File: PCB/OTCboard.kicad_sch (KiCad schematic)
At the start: 0 parts

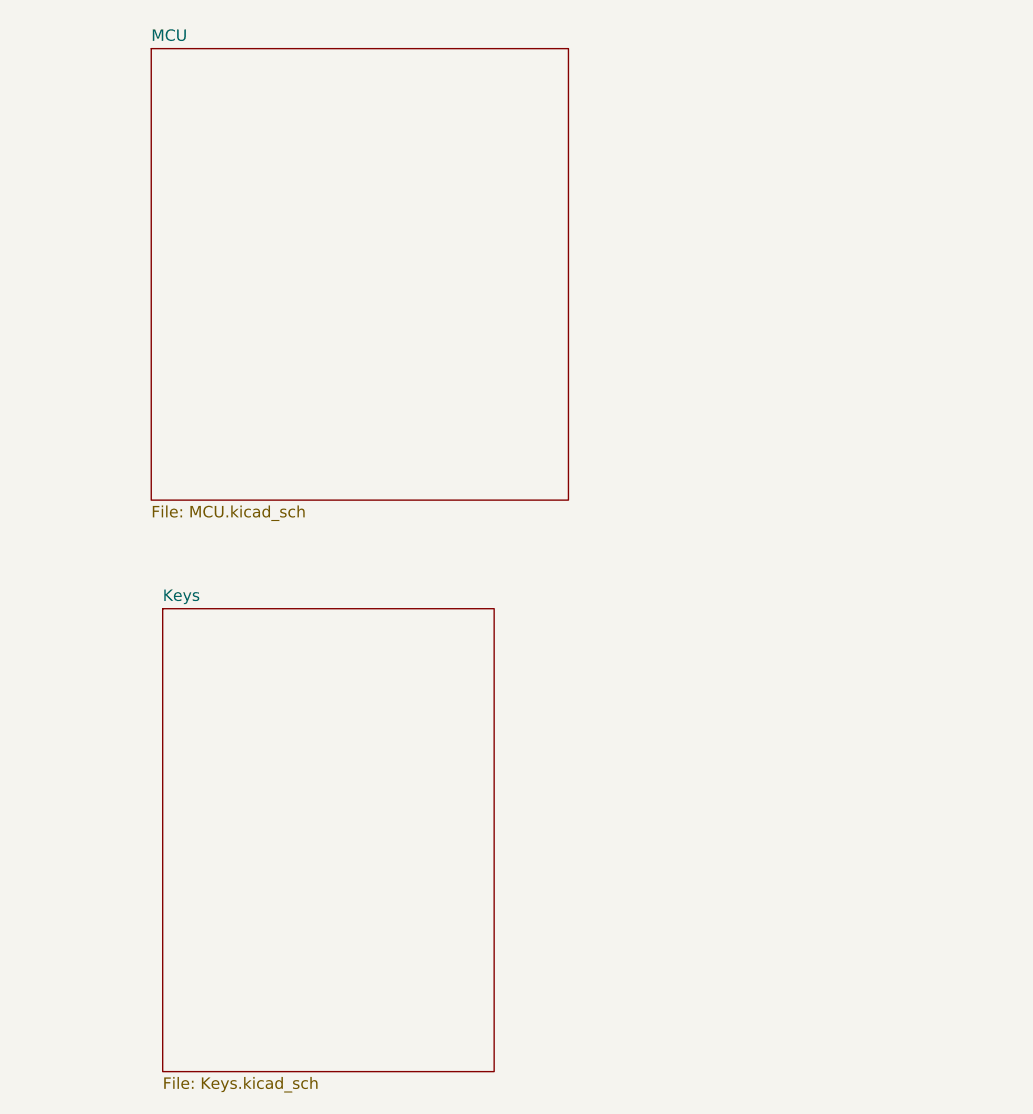
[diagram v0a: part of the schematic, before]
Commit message: switching to hall effect for now
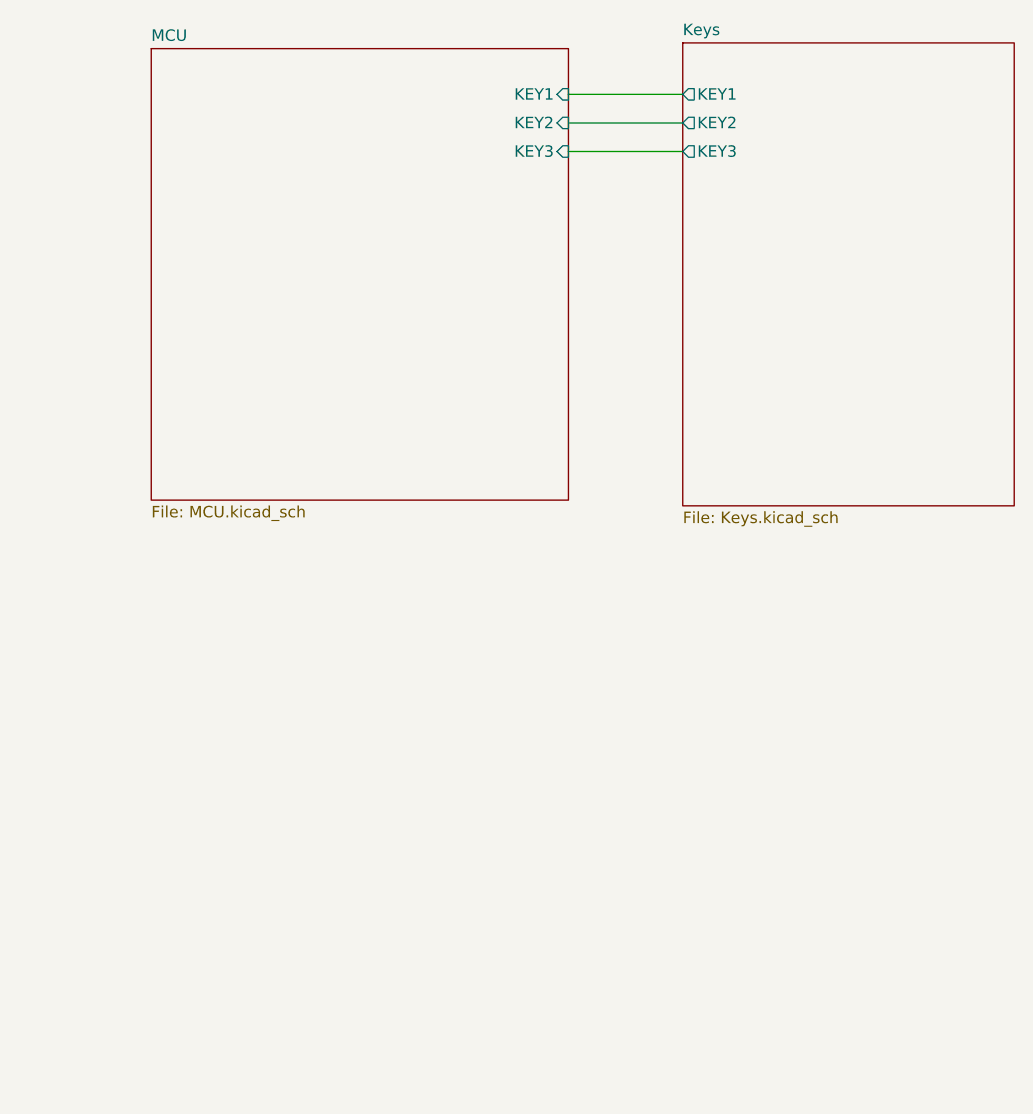
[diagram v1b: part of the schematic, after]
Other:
- sheet Keys ports: added KEY1, KEY2, KEY3; removed none
- sheet MCU ports: added KEY1, KEY2, KEY3; removed none
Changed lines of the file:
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@@
 	(generator_version "9.0")
 	(paper "A4")
+	(wire
+		(pts
+			(xy 137.795 30.48) (xy 150.495 30.48)
+		)
+		(stroke
+			(width 0)
+			(type default)
+		)
+	)
+	(wire
+		(pts
+			(xy 137.795 24.13) (xy 150.495 24.13)
+		)
+		(stroke
+			(width 0)
+			(type default)
+		)
+	)
+	(wire
+		(pts
+			(xy 137.795 27.305) (xy 150.495 27.305)
+		)
+		(stroke
+			(width 0)
+			(type default)
+		)
+	)
 	(sheet
 		(at 91.44 19.05)
@@
 			)
 		)
+		(pin "KEY1" input
+			(at 137.795 24.13 0)
+			(effects
+				(font
+					(size 1.27 1.27)
+				)
+				(justify right)
+			)
+		)
+		(pin "KEY2" input
+			(at 137.795 27.305 0)
+			(effects
+				(font
+					(size 1.27 1.27)
+				)
+				(justify right)
+			)
+		)
+		(pin "KEY3" input
+			(at 137.795 30.48 0)
+			(effects
+				(font
+					(size 1.27 1.27)
+				)
+				(justify right)
+			)
+		)
 		(instances
 			(project "OTCboard"
@@
 	)
 	(sheet
-		(at 92.71 81.28)
+		(at 150.495 18.415)
 		(size 36.83 51.435)
 		(exclude_from_sim no)
@@
 		)
 		(property "Sheetname" "Keys"
-			(at 92.71 80.5684 0)
+			(at 150.495 17.7034 0)
 			(effects
 				(font
@@
 		)
 		(property "Sheetfile" "Keys.kicad_sch"
-			(at 92.71 133.2996 0)
+			(at 150.495 70.4346 0)
 			(effects
 				(font
@@
 			)
 		)
+		(pin "KEY1" output
+			(at 150.495 24.13 180)
+			(effects
+				(font
+					(size 1.27 1.27)
+				)
+				(justify left)
+			)
+		)
+		(pin "KEY2" output
+			(at 150.495 27.305 180)
+			(effects
+				(font
+					(size 1.27 1.27)
+				)
+				(justify left)
+			)
+		)
+		(pin "KEY3" output
+			(at 150.495 30.48 180)
+			(effects
+				(font
+					(size 1.27 1.27)
+				)
+				(justify left)
+			)
+		)

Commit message: cramming for portfolio
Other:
- added sheet LEDs (LEDs.kicad_sch)
- sheet MCU ports: added AddressableLEDs, BL, CS, DC, MOSI, RES, SCK, USB_D+, USB_D-; removed none

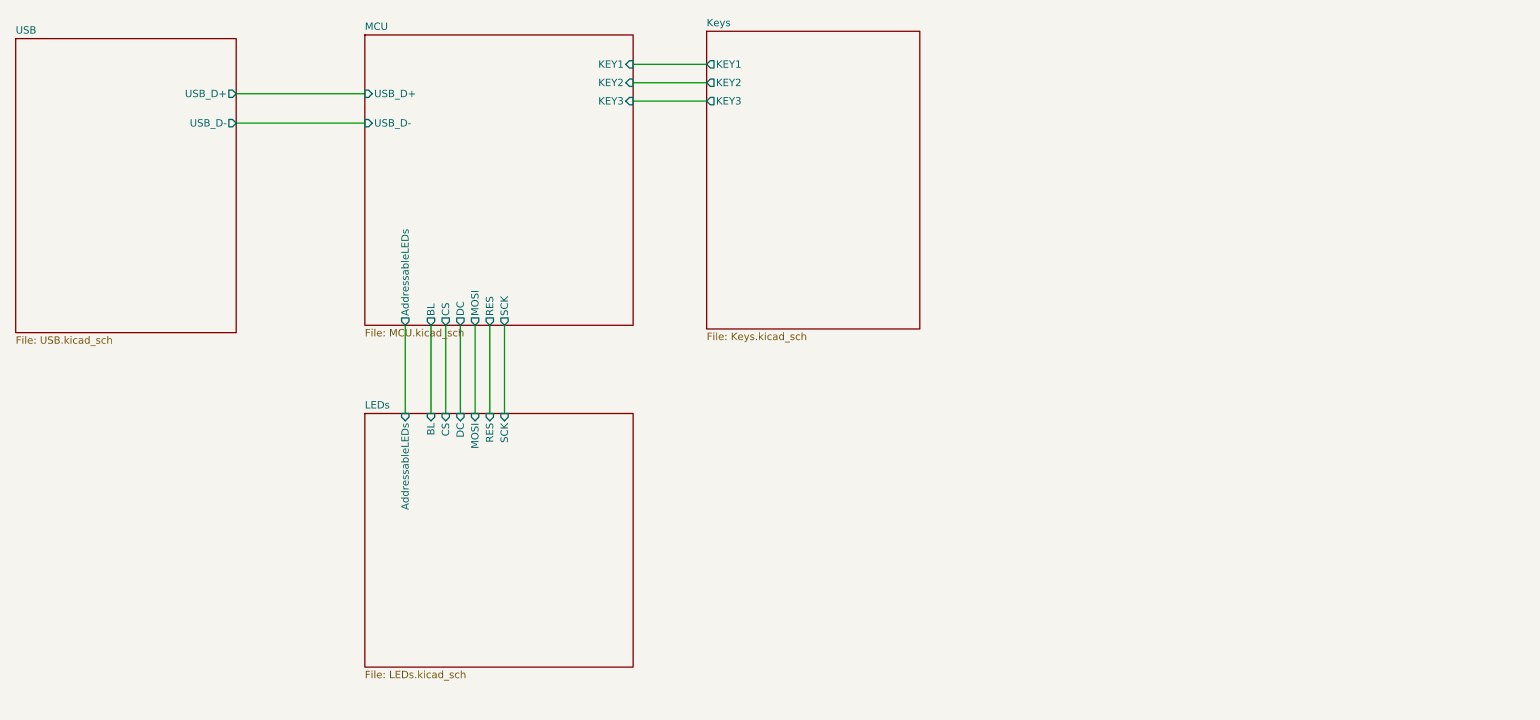
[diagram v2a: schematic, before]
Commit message: only need to find boot and reset footprints
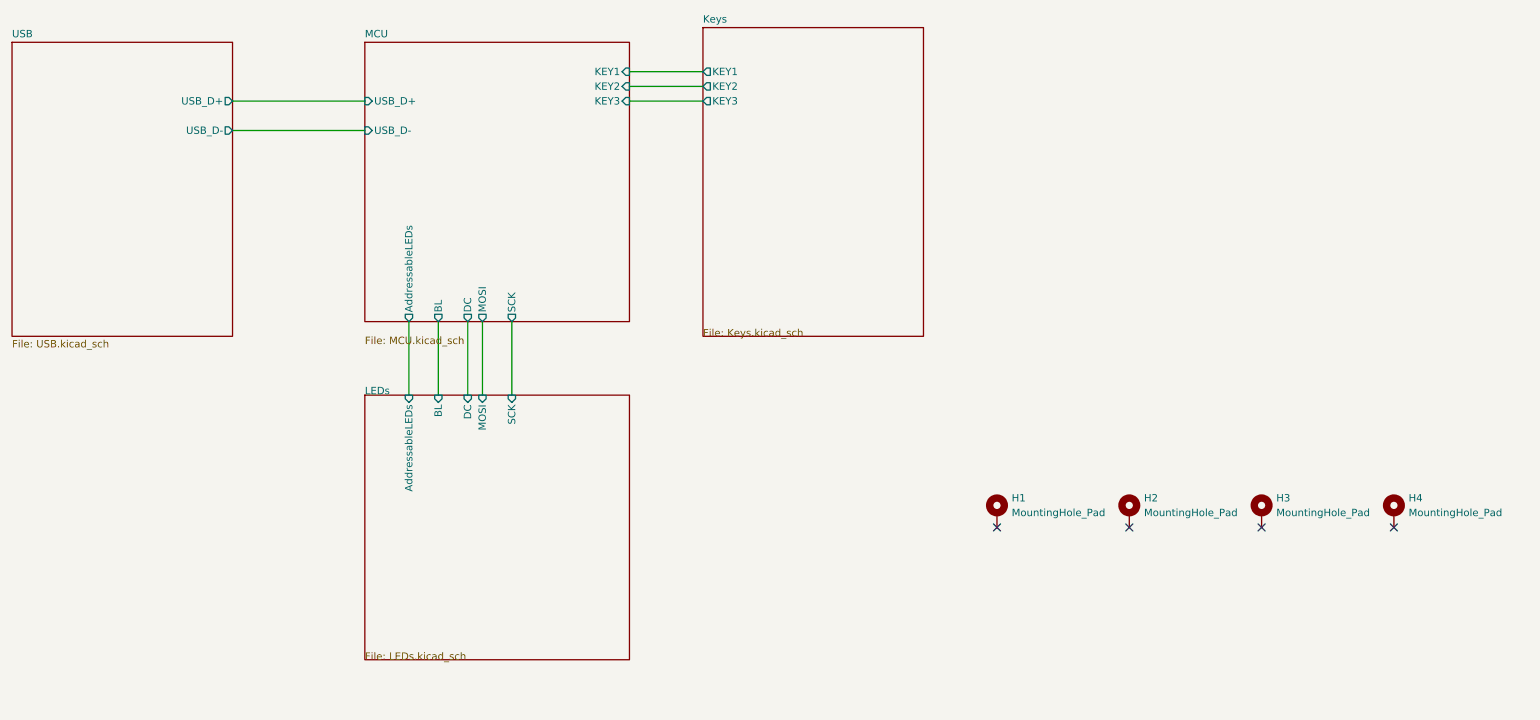
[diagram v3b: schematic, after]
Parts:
- added H1, H2, H3, H4: MountingHole_Pad, MountingHole:MountingHole_3.2mm_M3_Pad_TopBottom, symbol Mechanical:MountingHole_Pad
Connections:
- no-connect marks 0 -> 4
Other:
- sheet LEDs ports: added none; removed CS, RES
- sheet MCU ports: added none; removed CS, RES

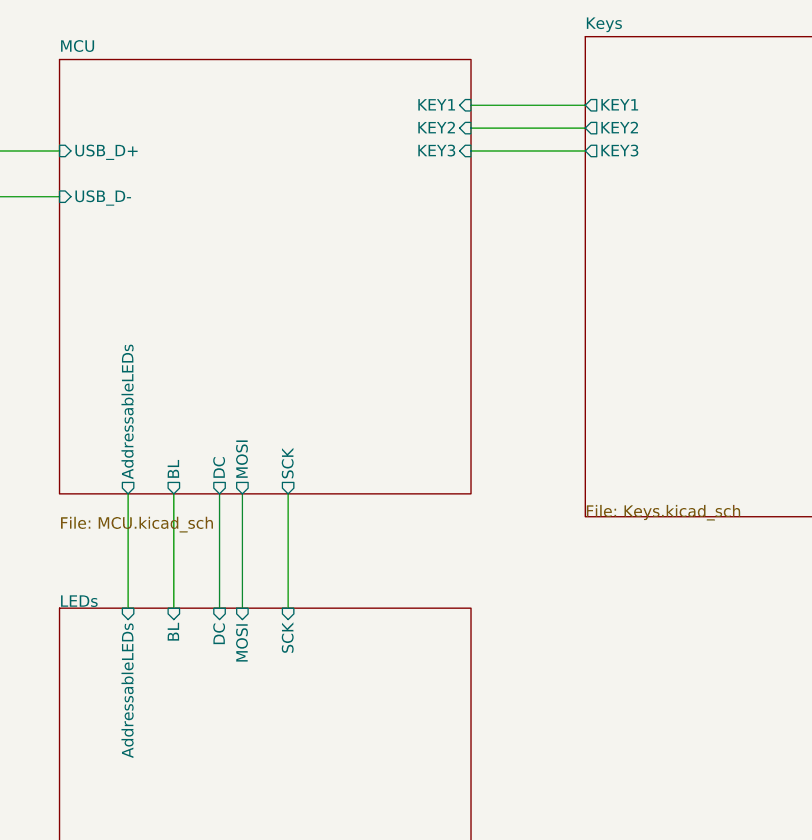
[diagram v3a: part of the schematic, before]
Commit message: changing to wasd
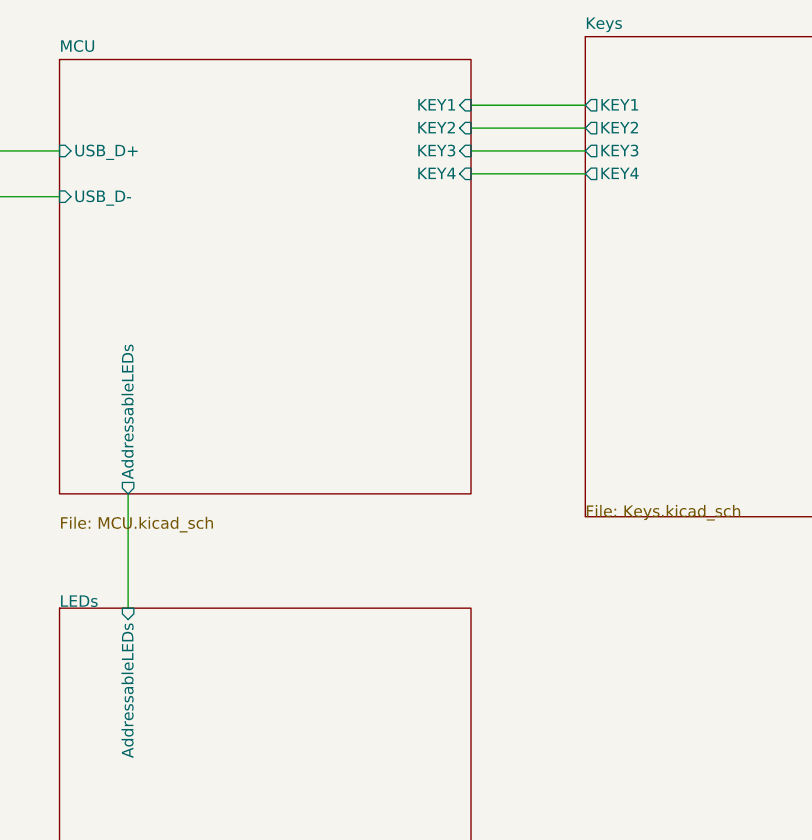
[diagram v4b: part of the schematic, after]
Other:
- sheet Keys ports: added KEY4; removed none
- sheet LEDs ports: added none; removed BL, DC, MOSI, SCK
- sheet MCU ports: added KEY4; removed BL, DC, MOSI, SCK
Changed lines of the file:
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@@
-	(wire
-		(pts
-			(xy 111.76 68.58) (xy 111.76 81.28)
-		)
-		(stroke
-			(width 0)
-			(type default)
-		)
-	)
-	(wire
-		(pts
-			(xy 109.22 68.58) (xy 109.22 81.28)
-		)
-		(stroke
-			(width 0)
-			(type default)
-		)
-	)
 	(wire
 		(pts
@@
 	(wire
 		(pts
-			(xy 104.14 68.58) (xy 104.14 81.28)
+			(xy 137.16 33.02) (xy 149.86 33.02)
 		)
 		(stroke
@@
 		(pts
 			(xy 137.16 27.94) (xy 149.86 27.94)
-		)
-		(stroke
-			(width 0)
-			(type default)
-		)
-	)
-	(wire
-		(pts
-			(xy 116.84 68.58) (xy 116.84 81.28)
 		)
 		(stroke
@@
 			)
 		)
-		(pin "BL" output
-			(at 104.14 68.58 270)
-			(effects
-				(font
-					(size 1.27 1.27)
-				)
-				(justify left)
-			)
-		)
-		(pin "DC" output
-			(at 109.22 68.58 270)
-			(effects
-				(font
-					(size 1.27 1.27)
-				)
-				(justify left)
-			)
-		)
-		(pin "MOSI" output
-			(at 111.76 68.58 270)
-			(effects
-				(font
-					(size 1.27 1.27)
-				)
-				(justify left)
-			)
-		)
-		(pin "SCK" output
-			(at 116.84 68.58 270)
-			(effects
-				(font
-					(size 1.27 1.27)
-				)
-				(justify left)
-			)
-		)
 		(pin "USB_D+" input
 			(at 91.44 30.48 180)
@@
 				)
 				(justify left)
+			)
+		)
+		(pin "KEY4" input
+			(at 137.16 33.02 0)
+			(effects
+				(font
+					(size 1.27 1.27)
+				)
+				(justify right)
 			)
 		)
@@
 			)
 		)
+		(pin "KEY4" output
+			(at 149.86 33.02 180)
+			(effects
+				(font
+					(size 1.27 1.27)
+				)
+				(justify left)
+			)
+		)
 		(instances
 			(project "OTCboard"
@@
 			(effects
 				(font
-					(size 1.27 1.27)
-				)
-				(justify right)
-			)
-		)
-		(pin "BL" input
-			(at 104.14 81.28 90)
-			(effects
-				(font
-					(size 1.27 1.27)
-				)
-				(justify right)
-			)
-		)
-		(pin "DC" input
-			(at 109.22 81.28 90)
-			(effects
-				(font
-					(size 1.27 1.27)
-				)
-				(justify right)
-			)
-		)
-		(pin "MOSI" input
-			(at 111.76 81.28 90)
-			(effects
-				(font
-					(size 1.27 1.27)
-				)
-				(justify right)
-			)
-		)
-		(pin "SCK" input
-			(at 116.84 81.28 90)
-			(effects
-				(font
